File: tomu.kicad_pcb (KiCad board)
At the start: 2 copper layers, 13 x 11 mm, 16 parts, among them P1 DEBUG, P3 USB-PCB, U1 MKL27Z256VFM4, U2 ateccXXXa

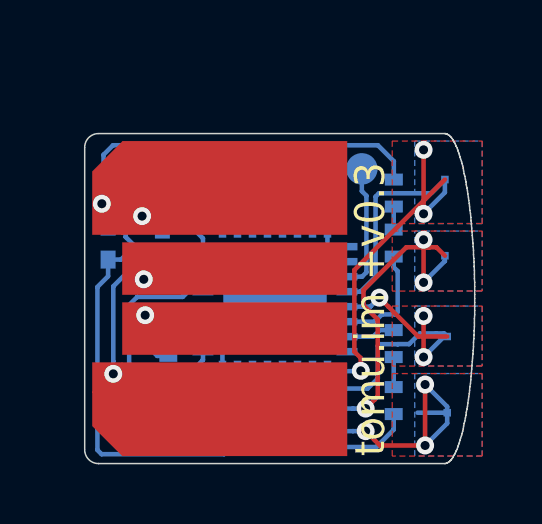
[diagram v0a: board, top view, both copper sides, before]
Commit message: Making the gnd traces thicker.
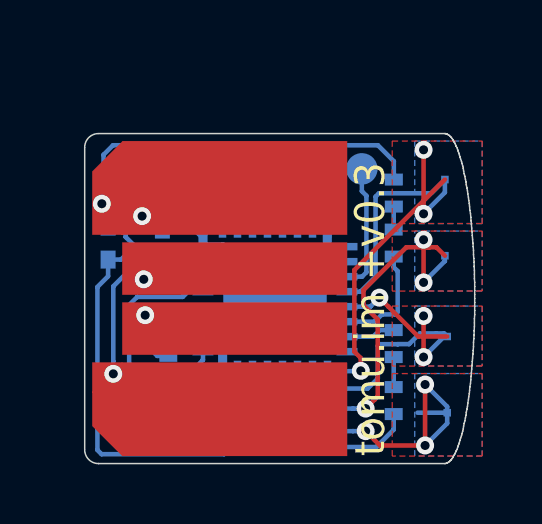
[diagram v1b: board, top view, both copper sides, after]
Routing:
- net GND: track 27.8 -> 35.3 mm
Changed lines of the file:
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@@
     (thickness 1.6)
     (drawings 179)
-    (tracks 262)
+    (tracks 276)
     (zones 0)
     (modules 16)
@@
   )
   (setup
-    (last_trace_width 0.1524)
+    (last_trace_width 0.3048)
     (user_trace_width 0.0254)
     (user_trace_width 0.1016)
@@
   (gr_line (start 30 23.77) (end 30 23.63) (layer Edge.Cuts) (width 0.05))
   (gr_line (start 30 23.63) (end 30 23.5) (layer Edge.Cuts) (width 0.05))
-  (segment (start 21.5926 25.9204) (end 21.5926 26.844) (width 0.1524) (layer B.Cu) (net 1))
-  (segment (start 21.5926 26.844) (end 21.2401 27.1965) (width 0.1524) (layer B.Cu) (net 1))
-  (segment (start 17.78 21.0996) (end 17.78 20.54785) (width 0.1524) (layer B.Cu) (net 1))
-  (segment (start 17.78 20.54785) (end 17.571506 20.339356) (width 0.1524) (layer B.Cu) (net 1))
+  (segment (start 17.571506 20.339356) (end 17.571506 20.891106) (width 0.3048) (layer B.Cu) (net 1))
+  (segment (start 17.571506 20.891106) (end 17.78 21.0996) (width 0.3048) (layer B.Cu) (net 1))
+  (segment (start 19.3526 26.809) (end 19.9776 26.809) (width 0.3048) (layer B.Cu) (net 1))
+  (segment (start 19.9776 26.809) (end 20.3651 27.1965) (width 0.3048) (layer B.Cu) (net 1))
+  (segment (start 21.5926 25.9204) (end 21.2401 26.2729) (width 0.3048) (layer B.Cu) (net 1))
+  (segment (start 21.2401 26.2729) (end 21.2401 27.1965) (width 0.3048) (layer B.Cu) (net 1))
+  (segment (start 21.5926 25.9204) (end 21.59 25.923) (width 0.3048) (layer B.Cu) (net 1))
+  (segment (start 21.5926 25.9204) (end 21.597401 25.915599) (width 0.3048) (layer B.Cu) (net 1))
+  (segment (start 21.597401 25.915599) (end 21.597401 25.265599) (width 0.3048) (layer B.Cu) (net 1))
+  (segment (start 21.597401 25.265599) (end 22.4801 24.3829) (width 0.3048) (layer B.Cu) (net 1))
+  (segment (start 20.9426 24.7704) (end 22.0926 24.7704) (width 0.3048) (layer B.Cu) (net 1))
+  (segment (start 24.903 20.193) (end 24.903 19.2422) (width 0.3048) (layer B.Cu) (net 1))
+  (segment (start 24.903 19.2422) (end 24.9682 19.177) (width 0.3048) (layer B.Cu) (net 1))
+  (segment (start 25.0926 21.1204) (end 25.087799 21.125201) (width 0.3048) (layer B.Cu) (net 1))
+  (segment (start 25.087799 21.125201) (end 25.087799 21.775201) (width 0.3048) (layer B.Cu) (net 1))
+  (segment (start 25.087799 21.775201) (end 24.2051 22.6579) (width 0.3048) (layer B.Cu) (net 1))
+  (segment (start 20.9426 21.7704) (end 20.947401 21.775201) (width 0.3048) (layer B.Cu) (net 1))
+  (segment (start 20.947401 21.775201) (end 21.597401 21.775201) (width 0.3048) (layer B.Cu) (net 1))
+  (segment (start 21.597401 21.775201) (end 22.4801 22.6579) (width 0.3048) (layer B.Cu) (net 1))
+  (segment (start 19.59 21.2) (end 19.361611 21.2) (width 0.3048) (layer B.Cu) (net 1))
+  (segment (start 19.361611 21.2) (end 18.913411 20.7518) (width 0.3048) (layer B.Cu) (net 1))
+  (segment (start 20.9426 21.7704) (end 20.9426 21.3406) (width 0.3048) (layer B.Cu) (net 1))
+  (segment (start 20.9426 21.3406) (end 20.802 21.2) (width 0.3048) (layer B.Cu) (net 1))
+  (segment (start 20.802 21.2) (end 20.6496 21.2) (width 0.3048) (layer B.Cu) (net 1))
+  (segment (start 19.59 21.2) (end 20.6496 21.2) (width 0.3048) (layer B.Cu) (net 1))
   (segment (start 17.99577 20.339356) (end 17.571506 20.339356) (width 0.1524) (layer F.Cu) (net 1))
   (segment (start 18.500967 20.339356) (end 17.99577 20.339356) (width 0.1524) (layer F.Cu) (net 1))
@@
   (via (at 17.571506 20.339356) (size 0.6) (drill 0.3) (layers F.Cu B.Cu) (net 1))
   (segment (start 17.661598 19.825) (end 17.571506 19.915092) (width 0.1524) (layer F.Cu) (net 1))
-  (segment (start 19.59 21.2) (end 19.1876 21.2) (width 0.1524) (layer B.Cu) (net 1))
-  (segment (start 19.1876 21.2) (end 18.913411 20.925811) (width 0.1524) (layer B.Cu) (net 1))
-  (segment (start 18.913411 20.925811) (end 18.913411 20.7518) (width 0.1524) (layer B.Cu) (net 1))
   (via (at 18.913411 20.7518) (size 0.6) (drill 0.3) (layers F.Cu B.Cu) (net 1))
   (segment (start 20.3651 27.1965) (end 21.2401 27.1965) (width 0.1524) (layer B.Cu) (net 1))
@@
   (segment (start 22.4801 22.6579) (end 24.2051 22.6579) (width 0.1524) (layer B.Cu) (net 1))
   (segment (start 22.4801 24.3829) (end 22.4801 22.6579) (width 0.1524) (layer B.Cu) (net 1))
-  (segment (start 24.903 20.193) (end 24.903 19.2422) (width 0.1524) (layer B.Cu) (net 1))
   (segment (start 25.0926 21.1204) (end 25.0926 20.3826) (width 0.1524) (layer B.Cu) (net 1))
   (segment (start 25.0926 20.3826) (end 24.903 20.193) (width 0.1524) (layer B.Cu) (net 1))
@@
   (segment (start 22.4801 22.6579) (end 21.5926 21.7704) (width 0.1524) (layer B.Cu) (net 1))
   (segment (start 21.5926 21.7704) (end 20.9426 21.7704) (width 0.1524) (layer B.Cu) (net 1))
-  (segment (start 19.3526 26.809) (end 19.9776 26.809) (width 0.1524) (layer B.Cu) (net 1))
-  (segment (start 19.9776 26.809) (end 20.3651 27.1965) (width 0.1524) (layer B.Cu) (net 1))
   (segment (start 22.4801 24.3829) (end 21.5926 25.2704) (width 0.1524) (layer B.Cu) (net 1))
   (segment (start 21.5926 25.2704) (end 21.5926 25.9204) (width 0.1524) (layer B.Cu) (net 1))
-  (segment (start 20.9426 24.7704) (end 22.0926 24.7704) (width 0.1524) (layer B.Cu) (net 1))
   (segment (start 22.0926 24.7704) (end 22.4801 24.3829) (width 0.1524) (layer B.Cu) (net 1))
   (segment (start 25.0926 21.1204) (end 25.0926 21.7704) (width 0.1524) (layer B.Cu) (net 1))

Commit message: Improving the silkscreen.
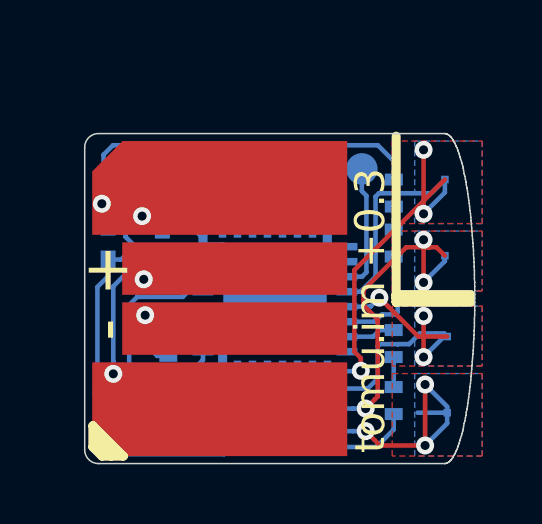
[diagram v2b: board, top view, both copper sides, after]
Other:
- board text added: "-"
- board text added: "tomu.im +0.3"
- board text removed: "tomu.im +v0.3"
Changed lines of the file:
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@@
     (area 9.247287 15.822599 139.107141 45.2)
     (thickness 1.6)
-    (drawings 179)
+    (drawings 212)
     (tracks 276)
     (zones 0)
@@
     (zone_45_only yes)
     (trace_min 0.1524)
-    (segment_width 0.1)
+    (segment_width 0.3)
     (edge_width 0.15)
     (via_size 0.6)
@@
       (net 16 /CAP0B))
   )
+  (gr_line (start 28.1432 23.3172) (end 28.1432 18.034) (layer B.SilkS) (width 0.3))
+  (gr_line (start 27.3812 23.622) (end 27.3812 18.0848) (layer F.SilkS) (width 0.3))
+  (gr_line (start 27.3812 23.4696) (end 29.8704 23.4696) (layer F.SilkS) (width 0.3))
+  (gr_line (start 30.0228 23.4696) (end 28.1432 23.4696) (layer B.SilkS) (width 0.3))
+  (gr_line (start 28.1432 23.622) (end 29.972 23.622) (layer B.SilkS) (width 0.3))
+  (gr_line (start 28.1432 23.3172) (end 28.1432 23.622) (layer B.SilkS) (width 0.3))
+  (gr_line (start 29.972 23.3172) (end 28.1432 23.3172) (layer B.SilkS) (width 0.3))
+  (gr_line (start 27.3812 23.622) (end 27.3812 23.368) (layer F.SilkS) (width 0.3))
+  (gr_line (start 27.3812 23.622) (end 29.8704 23.622) (layer F.SilkS) (width 0.3))
+  (gr_line (start 27.3812 23.368) (end 29.8704 23.368) (layer F.SilkS) (width 0.3))
+  (gr_line (start 17.8816 28.7528) (end 17.3228 28.1432) (layer F.SilkS) (width 0.3))
+  (gr_line (start 17.272 28.448) (end 17.272 27.7368) (layer F.SilkS) (width 0.3))
+  (gr_line (start 17.5768 28.7528) (end 17.272 28.448) (layer F.SilkS) (width 0.3))
+  (gr_line (start 18.288 28.7528) (end 17.5768 28.7528) (layer F.SilkS) (width 0.3))
+  (gr_line (start 17.272 27.7368) (end 18.288 28.7528) (layer F.SilkS) (width 0.3))
+  (gr_text - (at 17.7292 24.5364 90) (layer F.SilkS)
+    (effects (font (size 1.5 1.5) (thickness 0.3)))
+  )
+  (gr_text + (at 17.7292 22.5552 90) (layer F.SilkS)
+    (effects (font (size 1.5 1.5) (thickness 0.3)))
+  )
+  (gr_line (start 18.0848 19.3548) (end 18.0848 19.6596) (layer B.SilkS) (width 0.3))
+  (gr_line (start 19.1008 19.6596) (end 19.1008 19.3548) (layer B.SilkS) (width 0.3))
+  (gr_line (start 18.0848 19.6596) (end 19.1008 19.6596) (layer B.SilkS) (width 0.3))
+  (gr_line (start 20.1676 28.194) (end 19.9136 28.194) (layer B.SilkS) (width 0.3))
+  (gr_line (start 20.1676 28.6004) (end 20.1676 28.194) (layer B.SilkS) (width 0.3))
+  (gr_line (start 19.9136 28.6004) (end 20.1676 28.6004) (layer B.SilkS) (width 0.3))
+  (gr_line (start 19.9136 28.194) (end 19.9136 28.6004) (layer B.SilkS) (width 0.3))
+  (gr_line (start 21.8948 24.9428) (end 21.59 24.9428) (layer B.SilkS) (width 0.3))
+  (gr_line (start 21.8948 25.2476) (end 21.8948 24.9428) (layer B.SilkS) (width 0.3))
+  (gr_line (start 21.59 25.2476) (end 21.8948 25.2476) (layer B.SilkS) (width 0.3))
+  (gr_line (start 21.59 24.9428) (end 21.59 25.2476) (layer B.SilkS) (width 0.3))
+  (gr_line (start 20.4216 26.1112) (end 21.0312 25.908) (layer B.SilkS) (width 0.3))
+  (gr_line (start 21.4376 26.1112) (end 20.4216 26.1112) (layer B.SilkS) (width 0.3))
+  (gr_line (start 21.4376 26.1112) (end 21.4376 26.1112) (layer B.SilkS) (width 0.3))
+  (gr_line (start 20.9296 25.6032) (end 21.4376 26.1112) (layer B.SilkS) (width 0.3))
+  (gr_line (start 20.9296 25.6032) (end 20.4216 26.1112) (layer B.SilkS) (width 0.3))
   (gr_text "N\n" (at 26.2636 18.4912 90) (layer B.SilkS)
     (effects (font (size 0.6 0.6) (thickness 0.15)) (justify mirror))
@@
     (arrow2b (pts (xy 16.383 26.416) (xy 16.969421 27.542504)))
   )
-  (gr_text "tomu.im +v0.3" (at 26.5176 28.7528 90) (layer F.SilkS)
-    (effects (font (size 1 0.95) (thickness 0.2375)) (justify left))
+  (gr_text "tomu.im +0.3" (at 26.5176 28.6512 90) (layer F.SilkS)
+    (effects (font (size 1 1) (thickness 0.25)) (justify left))
   )
   (gr_line (start 21.44 23.99) (end 21.12 23.99) (layer Dwgs.User) (width 0.1016))

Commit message: Setting version to +0.0
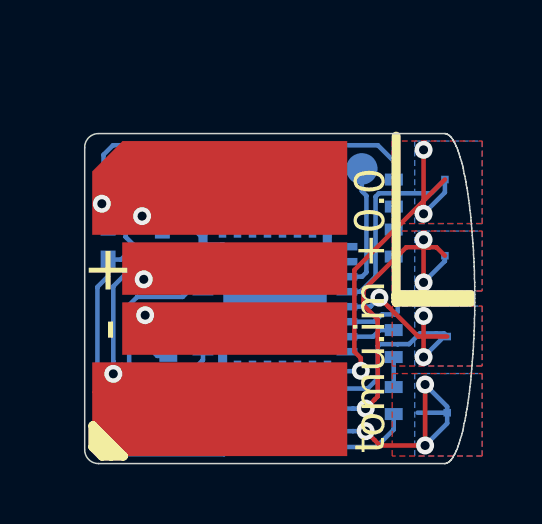
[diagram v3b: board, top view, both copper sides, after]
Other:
- board text added: "tomu.im +0.0"
- board text removed: "tomu.im +0.3"
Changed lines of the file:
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@@
     (arrow2b (pts (xy 16.383 26.416) (xy 16.969421 27.542504)))
   )
-  (gr_text "tomu.im +0.3" (at 26.5176 28.6512 90) (layer F.SilkS)
+  (gr_text "tomu.im +0.0" (at 26.5176 28.6512 90) (layer F.SilkS)
     (effects (font (size 1 1) (thickness 0.25)) (justify left))
   )

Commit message: Adding slot.
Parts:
- added REF**: Measurement_Point_Round-TH_Small, usb-pcb:slot, F.Cu at (29.1, 23.5)
- moved W2 0.34 mm to (29.0, 25.1)
- moved W1 0.33 mm to (29.0, 19.2)
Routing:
- net /CAP1B: track 11.7 -> 9.14 mm
- net /CAP1A: track 13.3 -> 11.4 mm
- net /CAP0A: track 18.8 -> 16.9 mm
- net /CAP0B: track 13.6 -> 12.3 mm
